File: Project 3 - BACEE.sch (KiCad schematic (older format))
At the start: 10 parts

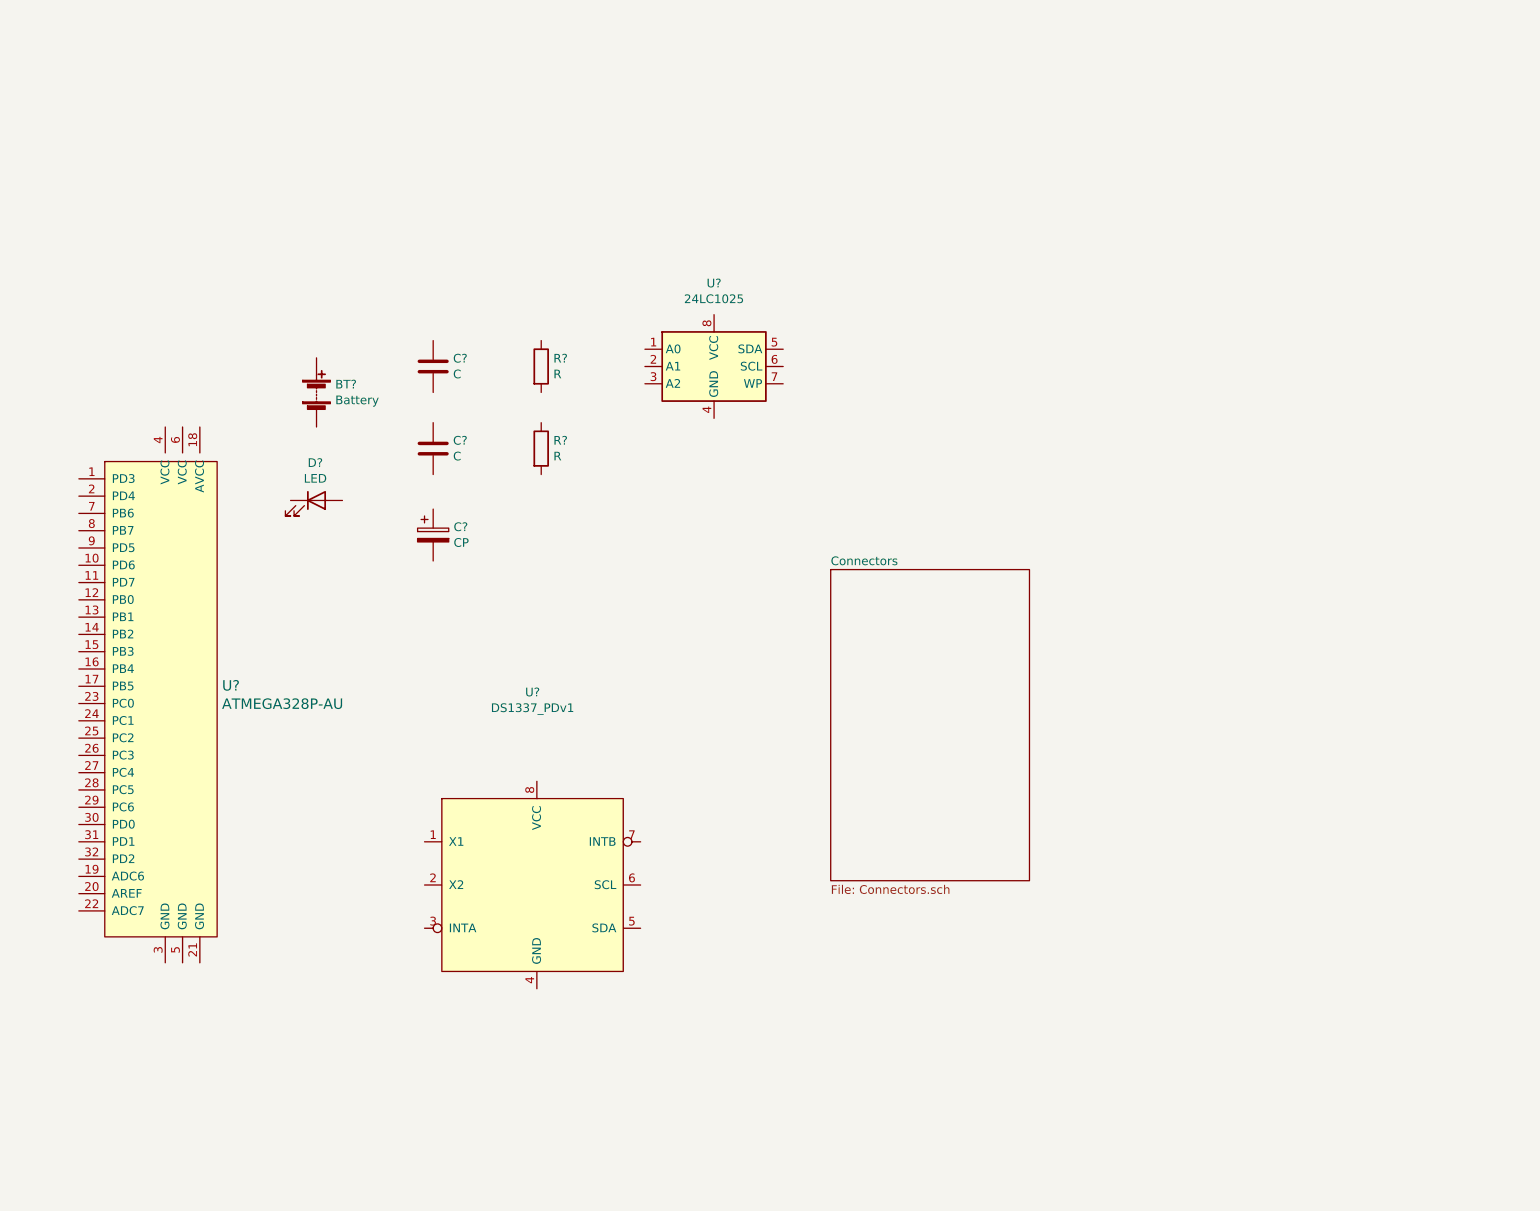
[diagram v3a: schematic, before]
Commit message: Added missing crystals.
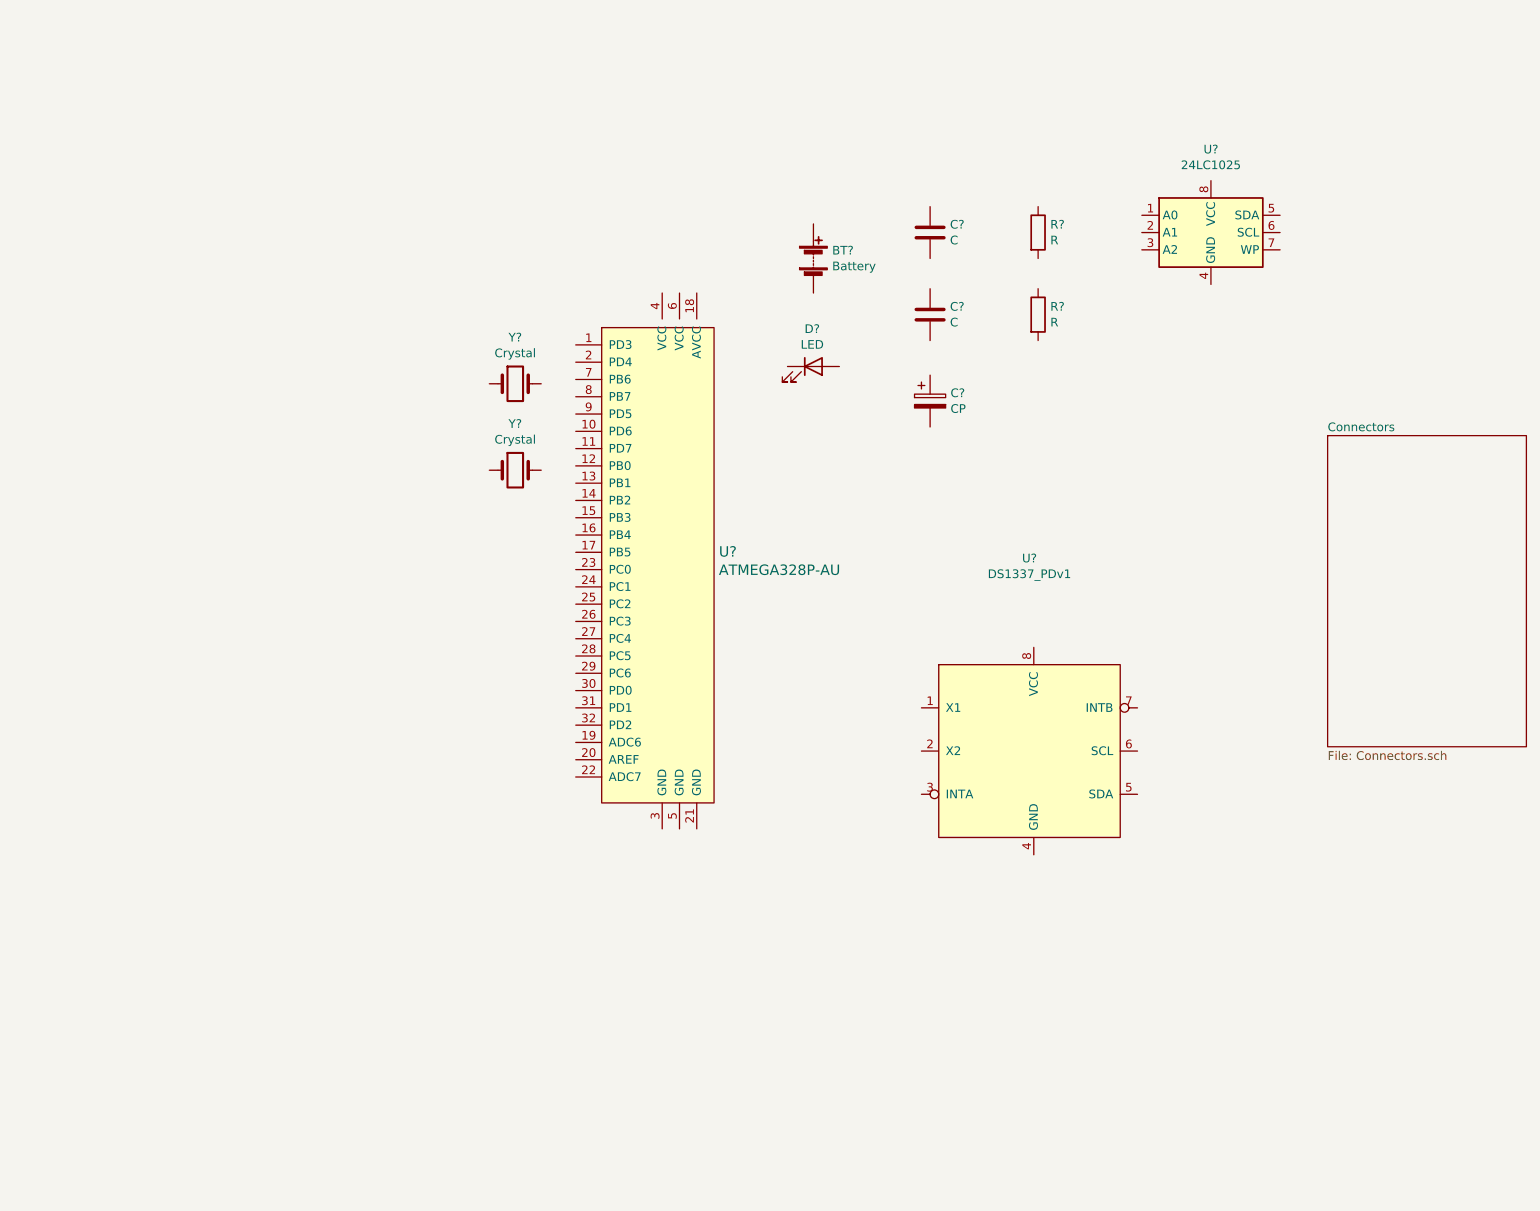
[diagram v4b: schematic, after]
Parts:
- added Y? (x2): Crystal, symbol Device:Crystal
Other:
- moved on the sheet: BT?, C?, D?, R?, U?
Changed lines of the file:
@@
 L Device:Battery BT?
 U 1 1 5F0CDB03
-P 2500 3050
-F 0 "BT?" H 2608 3096 50  0000 L CNN
-F 1 "Battery" H 2608 3005 50  0000 L CNN
-F 2 "" V 2500 3110 50  0001 C CNN
-F 3 "~" V 2500 3110 50  0001 C CNN
-	1    2500 3050
+P 5375 2275
+F 0 "BT?" H 5483 2321 50  0000 L CNN
+F 1 "Battery" H 5483 2230 50  0000 L CNN
+F 2 "" V 5375 2335 50  0001 C CNN
+F 3 "~" V 5375 2335 50  0001 C CNN
+	1    5375 2275
 	1    0    0    -1
 $EndComp
@@
 L Device:C C?
 U 1 1 5F0CEA38
-P 3175 2900
-F 0 "C?" H 3290 2946 50  0000 L CNN
-F 1 "C" H 3290 2855 50  0000 L CNN
-F 2 "" H 3213 2750 50  0001 C CNN
-F 3 "~" H 3175 2900 50  0001 C CNN
-	1    3175 2900
+P 6050 2125
+F 0 "C?" H 6165 2171 50  0000 L CNN
+F 1 "C" H 6165 2080 50  0000 L CNN
+F 2 "" H 6088 1975 50  0001 C CNN
+F 3 "~" H 6050 2125 50  0001 C CNN
+	1    6050 2125
 	1    0    0    -1
 $EndComp
@@
 L Device:C C?
 U 1 1 5F0CF2D4
-P 3175 3375
-F 0 "C?" H 3290 3421 50  0000 L CNN
-F 1 "C" H 3290 3330 50  0000 L CNN
-F 2 "" H 3213 3225 50  0001 C CNN
-F 3 "~" H 3175 3375 50  0001 C CNN
-	1    3175 3375
+P 6050 2600
+F 0 "C?" H 6165 2646 50  0000 L CNN
+F 1 "C" H 6165 2555 50  0000 L CNN
+F 2 "" H 6088 2450 50  0001 C CNN
+F 3 "~" H 6050 2600 50  0001 C CNN
+	1    6050 2600
 	1    0    0    -1
 $EndComp
@@
 L Device:CP C?
 U 1 1 5F0CF8DC
-P 3175 3875
-F 0 "C?" H 3293 3921 50  0000 L CNN
-F 1 "CP" H 3293 3830 50  0000 L CNN
-F 2 "" H 3213 3725 50  0001 C CNN
-F 3 "~" H 3175 3875 50  0001 C CNN
-	1    3175 3875
+P 6050 3100
+F 0 "C?" H 6168 3146 50  0000 L CNN
+F 1 "CP" H 6168 3055 50  0000 L CNN
+F 2 "" H 6088 2950 50  0001 C CNN
+F 3 "~" H 6050 3100 50  0001 C CNN
+	1    6050 3100
 	1    0    0    -1
 $EndComp
@@
 L Device:LED D?
 U 1 1 5F0CFE76
-P 2500 3675
-F 0 "D?" H 2493 3892 50  0000 C CNN
-F 1 "LED" H 2493 3801 50  0000 C CNN
-F 2 "" H 2500 3675 50  0001 C CNN
-F 3 "~" H 2500 3675 50  0001 C CNN
-	1    2500 3675
+P 5375 2900
+F 0 "D?" H 5368 3117 50  0000 C CNN
+F 1 "LED" H 5368 3026 50  0000 C CNN
+F 2 "" H 5375 2900 50  0001 C CNN
+F 3 "~" H 5375 2900 50  0001 C CNN
+	1    5375 2900
 	1    0    0    -1
 $EndComp
@@
 L Device:R R?
 U 1 1 5F0D09EF
-P 3800 2900
-F 0 "R?" H 3870 2946 50  0000 L CNN
-F 1 "R" H 3870 2855 50  0000 L CNN
-F 2 "" V 3730 2900 50  0001 C CNN
-F 3 "~" H 3800 2900 50  0001 C CNN
-	1    3800 2900
+P 6675 2125
+F 0 "R?" H 6745 2171 50  0000 L CNN
+F 1 "R" H 6745 2080 50  0000 L CNN
+F 2 "" V 6605 2125 50  0001 C CNN
+F 3 "~" H 6675 2125 50  0001 C CNN
+	1    6675 2125
 	1    0    0    -1
 $EndComp
@@
 L Device:R R?
 U 1 1 5F0D11B8
-P 3800 3375
-F 0 "R?" H 3870 3421 50  0000 L CNN
-F 1 "R" H 3870 3330 50  0000 L CNN
-F 2 "" V 3730 3375 50  0001 C CNN
-F 3 "~" H 3800 3375 50  0001 C CNN
-	1    3800 3375
+P 6675 2600
+F 0 "R?" H 6745 2646 50  0000 L CNN
+F 1 "R" H 6745 2555 50  0000 L CNN
+F 2 "" V 6605 2600 50  0001 C CNN
+F 3 "~" H 6675 2600 50  0001 C CNN
+	1    6675 2600
 	1    0    0    -1
 $EndComp
@@
 L Memory_EEPROM:24LC1025 U?
 U 1 1 5F0D1B59
-P 4800 2900
-F 0 "U?" H 4800 3381 50  0000 C CNN
-F 1 "24LC1025" H 4800 3290 50  0000 C CNN
-F 2 "" H 4800 2900 50  0001 C CNN
-F 3 "http://ww1.microchip.com/downloads/en/DeviceDoc/21941B.pdf" H 4800 2900 50  0001 C CNN
-	1    4800 2900
+P 7675 2125
+F 0 "U?" H 7675 2606 50  0000 C CNN
+F 1 "24LC1025" H 7675 2515 50  0000 C CNN
+F 2 "" H 7675 2125 50  0001 C CNN
+F 3 "http://ww1.microchip.com/downloads/en/DeviceDoc/21941B.pdf" H 7675 2125 50  0001 C CNN
+	1    7675 2125
 	1    0    0    -1
 $EndComp
 $Sheet
-S 5475 4075 1150 1800
+S 8350 3300 1150 1800
 U 5F0D3531
 F0 "Connectors" 50
@@
 L dk_Embedded-Microcontrollers:ATMEGA328P-AU U?
 U 1 1 5F0D825C
-P 1625 4850
-F 0 "U?" H 1953 4953 60  0000 L CNN
-F 1 "ATMEGA328P-AU" H 1953 4847 60  0000 L CNN
-F 2 "digikey-footprints:TQFP-32_7x7mm" H 1825 5050 60  0001 L CNN
-F 3 "http://www.microchip.com/mymicrochip/filehandler.aspx?ddocname=en608326" H 1825 5150 60  0001 L CNN
-F 4 "ATMEGA328P-AU-ND" H 1825 5250 60  0001 L CNN "Digi-Key_PN"
-F 5 "ATMEGA328P-AU" H 1825 5350 60  0001 L CNN "MPN"
-F 6 "Integrated Circuits (ICs)" H 1825 5450 60  0001 L CNN "Category"
-F 7 "Embedded - Microcontrollers" H 1825 5550 60  0001 L CNN "Family"
-F 8 "http://www.microchip.com/mymicrochip/filehandler.aspx?ddocname=en608326" H 1825 5650 60  0001 L CNN "DK_Datasheet_Link"
-F 9 "/product-detail/en/microchip-technology/ATMEGA328P-AU/ATMEGA328P-AU-ND/1832260" H 1825 5750 60  0001 L CNN "DK_Detail_Page"
-F 10 "IC MCU 8BIT 32KB FLASH 32TQFP" H 1825 5850 60  0001 L CNN "Description"
-F 11 "Microchip Technology" H 1825 5950 60  0001 L CNN "Manufacturer"
-F 12 "Active" H 1825 6050 60  0001 L CNN "Status"
-	1    1625 4850
+P 4500 4075
+F 0 "U?" H 4828 4178 60  0000 L CNN
+F 1 "ATMEGA328P-AU" H 4828 4072 60  0000 L CNN
+F 2 "digikey-footprints:TQFP-32_7x7mm" H 4700 4275 60  0001 L CNN
+F 3 "http://www.microchip.com/mymicrochip/filehandler.aspx?ddocname=en608326" H 4700 4375 60  0001 L CNN
+F 4 "ATMEGA328P-AU-ND" H 4700 4475 60  0001 L CNN "Digi-Key_PN"
+F 5 "ATMEGA328P-AU" H 4700 4575 60  0001 L CNN "MPN"
+F 6 "Integrated Circuits (ICs)" H 4700 4675 60  0001 L CNN "Category"
+F 7 "Embedded - Microcontrollers" H 4700 4775 60  0001 L CNN "Family"
+F 8 "http://www.microchip.com/mymicrochip/filehandler.aspx?ddocname=en608326" H 4700 4875 60  0001 L CNN "DK_Datasheet_Link"
+F 9 "/product-detail/en/microchip-technology/ATMEGA328P-AU/ATMEGA328P-AU-ND/1832260" H 4700 4975 60  0001 L CNN "DK_Detail_Page"
+F 10 "IC MCU 8BIT 32KB FLASH 32TQFP" H 4700 5075 60  0001 L CNN "Description"
+F 11 "Microchip Technology" H 4700 5175 60  0001 L CNN "Manufacturer"
+F 12 "Active" H 4700 5275 60  0001 L CNN "Status"
+	1    4500 4075
 	1    0    0    -1
 $EndComp
@@
 L Project3:DS1337_PDv1 U?
 U 1 1 5F0DBCFF
-P 3775 5900
-F 0 "U?" H 3750 7015 50  0000 C CNN
-F 1 "DS1337_PDv1" H 3750 6924 50  0000 C CNN
-F 2 "" H 3475 6250 50  0001 C CNN
-F 3 "https://datasheets.maximintegrated.com/en/ds/DS1337-DS1337C.pdf" H 3475 6250 50  0001 C CNN
-	1    3775 5900
+P 6650 5125
+F 0 "U?" H 6625 6240 50  0000 C CNN
+F 1 "DS1337_PDv1" H 6625 6149 50  0000 C CNN
+F 2 "" H 6350 5475 50  0001 C CNN
+F 3 "https://datasheets.maximintegrated.com/en/ds/DS1337-DS1337C.pdf" H 6350 5475 50  0001 C CNN
+	1    6650 5125
 	1    0    0    -1
 $EndComp
+$Comp
+L Device:Crystal Y?
+U 1 1 5F0E9423
+P 3650 3000
+F 0 "Y?" H 3650 3268 50  0000 C CNN
+F 1 "Crystal" H 3650 3177 50  0000 C CNN
+F 2 "" H 3650 3000 50  0001 C CNN
+F 3 "~" H 3650 3000 50  0001 C CNN
+	1    3650 3000
+	1    0    0    -1
+$EndComp
+$Comp
+L Device:Crystal Y?
+U 1 1 5F0EA205
+P 3650 3500
+F 0 "Y?" H 3650 3768 50  0000 C CNN
+F 1 "Crystal" H 3650 3677 50  0000 C CNN
+F 2 "" H 3650 3500 50  0001 C CNN
+F 3 "~" H 3650 3500 50  0001 C CNN
+	1    3650 3500
+	1    0    0    -1
+$EndComp
